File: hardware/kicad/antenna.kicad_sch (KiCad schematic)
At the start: 35 parts, among them J5 BWIPX-1-001E, J7 BWIPX-1-001E

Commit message: fix drc, layout and schematics
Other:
- note added: "Coplanar Waveguide With Ground Characteristic"
- note added: "Effective Dielectric Constant: 3.295 Characteristic Impedance: 49.9ohm"
- note added: "Relative Dielectric Constant: 4.56 Track Width : 0.33mm Gap Width : 0.2mm Dielectric Thickness : 0.1855mm"
- note added: "Trace Characteristic"
- note added: "Trace characteristics"
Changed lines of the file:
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@@
 	(title_block
 		(title "Antenna")
-		(date "2024-05-17")
-		(rev "1")
+		(date "2024-05-22")
+		(rev "2")
 		(company "Teapot Laboratories")
 	)
@@
 	(wire
 		(pts
-			(xy 85.09 121.793) (xy 81.28 121.793)
+			(xy 109.22 160.02) (xy 105.41 160.02)
 		)
 		(stroke
@@
 	(wire
 		(pts
-			(xy 85.09 117.983) (xy 85.09 121.793)
+			(xy 109.22 156.21) (xy 109.22 160.02)
 		)
 		(stroke
@@
 	)
 	(rectangle
+		(start 37.084 110.236)
+		(end 90.17 146.05)
+		(stroke
+			(width 0.5)
+			(type default)
+		)
+		(fill
+			(type none)
+		)
+	)
+	(rectangle
 		(start 93.345 38.735)
 		(end 279.4 146.05)
@@
 	)
 	(rectangle
-		(start 68.58 109.22)
-		(end 90.17 128.27)
+		(start 93.218 148.463)
+		(end 114.808 167.513)
 		(stroke
 			(width 0)
@@
 	(text "Sheets Connection"
 		(exclude_from_sim no)
-		(at 71.12 126.873 0)
+		(at 95.25 165.1 0)
 		(effects
 			(font
@@
 		)
 	)
+	(text "Trace characteristics"
+		(exclude_from_sim no)
+		(at 40.132 121.666 0)
+		(effects
+			(font
+				(size 1.27 1.27)
+				(thickness 0.254)
+				(bold yes)
+			)
+			(justify left bottom)
+		)
+	)
 	(text "EXT/TEST"
 		(exclude_from_sim no)
@@
 		)
 	)
+	(text "Coplanar Waveguide With Ground Characteristic"
+		(exclude_from_sim no)
+		(at 40.132 136.906 0)
+		(effects
+			(font
+				(size 1.27 1.27)
+				(thickness 0.254)
+				(bold yes)
+			)
+			(justify left bottom)
+		)
+	)
 	(text "GNSS Antenna Out"
 		(exclude_from_sim no)
@@
 		)
 	)
+	(text "Trace Characteristic"
+		(exclude_from_sim no)
+		(at 50.546 115.57 0)
+		(effects
+			(font
+				(size 2 2)
+				(thickness 0.4)
+				(bold yes)
+			)
+			(justify left bottom)
+		)
+	)
 	(text "place as close to the antenna feed"
 		(exclude_from_sim no)
@@
 		)
 	)
+	(text "Relative Dielectric Constant: 4.56\nTrack Width : 0.33mm\nGap Width : 0.2mm\nDielectric Thickness : 0.1855mm"
+		(exclude_from_sim no)
+		(at 40.132 131.064 0)
+		(effects
+			(font
+				(size 1.27 1.27)
+			)
+			(justify left bottom)
+		)
+	)
+	(text "Effective Dielectric Constant: 3.295\nCharacteristic Impedance: 49.9ohm"
+		(exclude_from_sim no)
+		(at 40.132 141.986 0)
+		(effects
+			(font
+				(size 1.27 1.27)
+			)
+			(justify left bottom)
+		)
+	)
 	(text "Matching Network\n"
 		(exclude_from_sim no)
@@
 	(hierarchical_label "+3V3"
 		(shape input)
-		(at 81.28 121.793 180)
+		(at 105.41 160.02 180)
 		(fields_autoplaced yes)
 		(effects
@@
 	(symbol
 		(lib_id "power:+3V3")
-		(at 85.09 117.983 0)
+		(at 109.22 156.21 0)
 		(mirror y)
 		(unit 1)
@@
 		(dnp no)
 		(property "Reference" "#PWR0114"
-			(at 85.09 121.793 0)
+			(at 109.22 160.02 0)
 			(effects
 				(font
@@
 		)
 		(property "Value" "+3V3"
-			(at 82.55 114.173 0)
+			(at 106.68 152.4 0)
 			(effects
 				(font
@@
 		)
 		(property "Footprint" ""
-			(at 85.09 117.983 0)
+			(at 109.22 156.21 0)
 			(effects
 				(font
@@
 		)
 		(property "Datasheet" ""
-			(at 85.09 117.983 0)
+			(at 109.22 156.21 0)
 			(effects
 				(font
@@
 		)
 		(property "Description" ""
-			(at 85.09 117.983 0)
+			(at 109.22 156.21 0)
 			(effects
 				(font

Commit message: finalizing board info
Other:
- note removed: "Coplanar Waveguide With Ground Characteristic"
- note removed: "Effective Dielectric Constant: 3.295 Characteristic Impedance: 49.9ohm"
- note removed: "Relative Dielectric Constant: 4.56 Track Width : 0.33mm Gap Width : 0.2mm Dielectric Thickness : 0.1855mm"
- note removed: "Trace Characteristic"
- note removed: "Trace characteristics"
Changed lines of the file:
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@@
 	(wire
 		(pts
-			(xy 109.22 160.02) (xy 105.41 160.02)
+			(xy 85.09 121.793) (xy 81.28 121.793)
 		)
 		(stroke
@@
 	(wire
 		(pts
-			(xy 109.22 156.21) (xy 109.22 160.02)
+			(xy 85.09 117.983) (xy 85.09 121.793)
 		)
 		(stroke
@@
 	)
 	(rectangle
-		(start 37.084 110.236)
-		(end 90.17 146.05)
-		(stroke
-			(width 0.5)
-			(type default)
-		)
-		(fill
-			(type none)
-		)
-	)
-	(rectangle
 		(start 93.345 38.735)
 		(end 279.4 146.05)
@@
 	)
 	(rectangle
-		(start 93.218 148.463)
-		(end 114.808 167.513)
+		(start 68.58 109.22)
+		(end 90.17 128.27)
 		(stroke
 			(width 0)
@@
 	(text "Sheets Connection"
 		(exclude_from_sim no)
-		(at 95.25 165.1 0)
+		(at 71.12 126.873 0)
 		(effects
 			(font
@@
 		)
 	)
-	(text "Trace characteristics"
-		(exclude_from_sim no)
-		(at 40.132 121.666 0)
-		(effects
-			(font
-				(size 1.27 1.27)
-				(thickness 0.254)
-				(bold yes)
-			)
-			(justify left bottom)
-		)
-	)
 	(text "EXT/TEST"
 		(exclude_from_sim no)
@@
 		)
 	)
-	(text "Coplanar Waveguide With Ground Characteristic"
-		(exclude_from_sim no)
-		(at 40.132 136.906 0)
-		(effects
-			(font
-				(size 1.27 1.27)
-				(thickness 0.254)
-				(bold yes)
-			)
-			(justify left bottom)
-		)
-	)
 	(text "GNSS Antenna Out"
 		(exclude_from_sim no)
@@
 		)
 	)
-	(text "Trace Characteristic"
-		(exclude_from_sim no)
-		(at 50.546 115.57 0)
-		(effects
-			(font
-				(size 2 2)
-				(thickness 0.4)
-				(bold yes)
-			)
-			(justify left bottom)
-		)
-	)
 	(text "place as close to the antenna feed"
 		(exclude_from_sim no)
@@
 		)
 	)
-	(text "Relative Dielectric Constant: 4.56\nTrack Width : 0.33mm\nGap Width : 0.2mm\nDielectric Thickness : 0.1855mm"
-		(exclude_from_sim no)
-		(at 40.132 131.064 0)
-		(effects
-			(font
-				(size 1.27 1.27)
-			)
-			(justify left bottom)
-		)
-	)
-	(text "Effective Dielectric Constant: 3.295\nCharacteristic Impedance: 49.9ohm"
-		(exclude_from_sim no)
-		(at 40.132 141.986 0)
-		(effects
-			(font
-				(size 1.27 1.27)
-			)
-			(justify left bottom)
-		)
-	)
 	(text "Matching Network\n"
 		(exclude_from_sim no)
@@
 	(hierarchical_label "+3V3"
 		(shape input)
-		(at 105.41 160.02 180)
+		(at 81.28 121.793 180)
 		(fields_autoplaced yes)
 		(effects
@@
 	(symbol
 		(lib_id "power:+3V3")
-		(at 109.22 156.21 0)
+		(at 85.09 117.983 0)
 		(mirror y)
 		(unit 1)
@@
 		(dnp no)
 		(property "Reference" "#PWR0114"
-			(at 109.22 160.02 0)
+			(at 85.09 121.793 0)
 			(effects
 				(font
@@
 		)
 		(property "Value" "+3V3"
-			(at 106.68 152.4 0)
+			(at 82.55 114.173 0)
 			(effects
 				(font
@@
 		)
 		(property "Footprint" ""
-			(at 109.22 156.21 0)
+			(at 85.09 117.983 0)
 			(effects
 				(font
@@
 		)
 		(property "Datasheet" ""
-			(at 109.22 156.21 0)
+			(at 85.09 117.983 0)
 			(effects
 				(font
@@
 		)
 		(property "Description" ""
-			(at 109.22 156.21 0)
+			(at 85.09 117.983 0)
 			(effects
 				(font

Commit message: Start Rev 3
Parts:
- removed C48, C49: DNP, Capacitor_SMD:C_0402_1005Metric, symbol Device:C_Small
- removed D3: ESD5651N, Diode_SMD:D_SOD-882, symbol Device:D_TVS
- removed E1: NN03-320, bwlc1a:NN03-320, symbol bwlc1a:NN03-320
- removed J5: BWIPX-1-001E, bwlc1a:BWIPX-1-001E, symbol bwlc1a:BWIPX-1-001E
- removed L1: 10n, Inductor_SMD:L_0603_1608Metric, symbol Device:L
- removed L2: 9n5, Inductor_SMD:L_0603_1608Metric, symbol Device:L
- removed R24, R35, R36, R37: 0, Resistor_SMD:R_0402_1005Metric, symbol Device:R_Small
- removed R38: 0, Resistor_SMD:R_0603_1608Metric, symbol Device:R_Small
- removed R40: DNP, Resistor_SMD:R_0402_1005Metric, symbol Device:R_Small
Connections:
- no-connect marks 3 -> 0

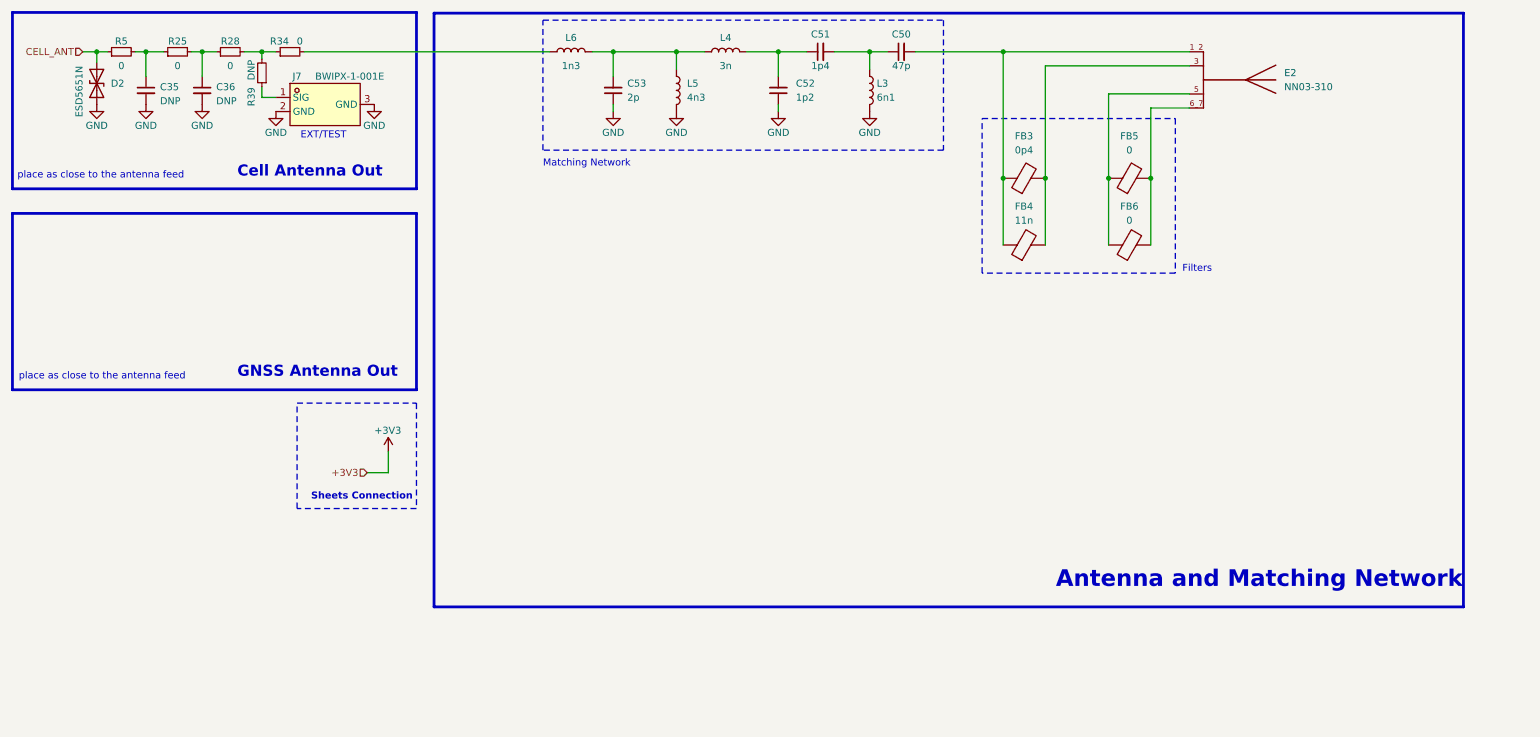
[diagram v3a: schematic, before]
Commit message: GNSS and Antenna Update
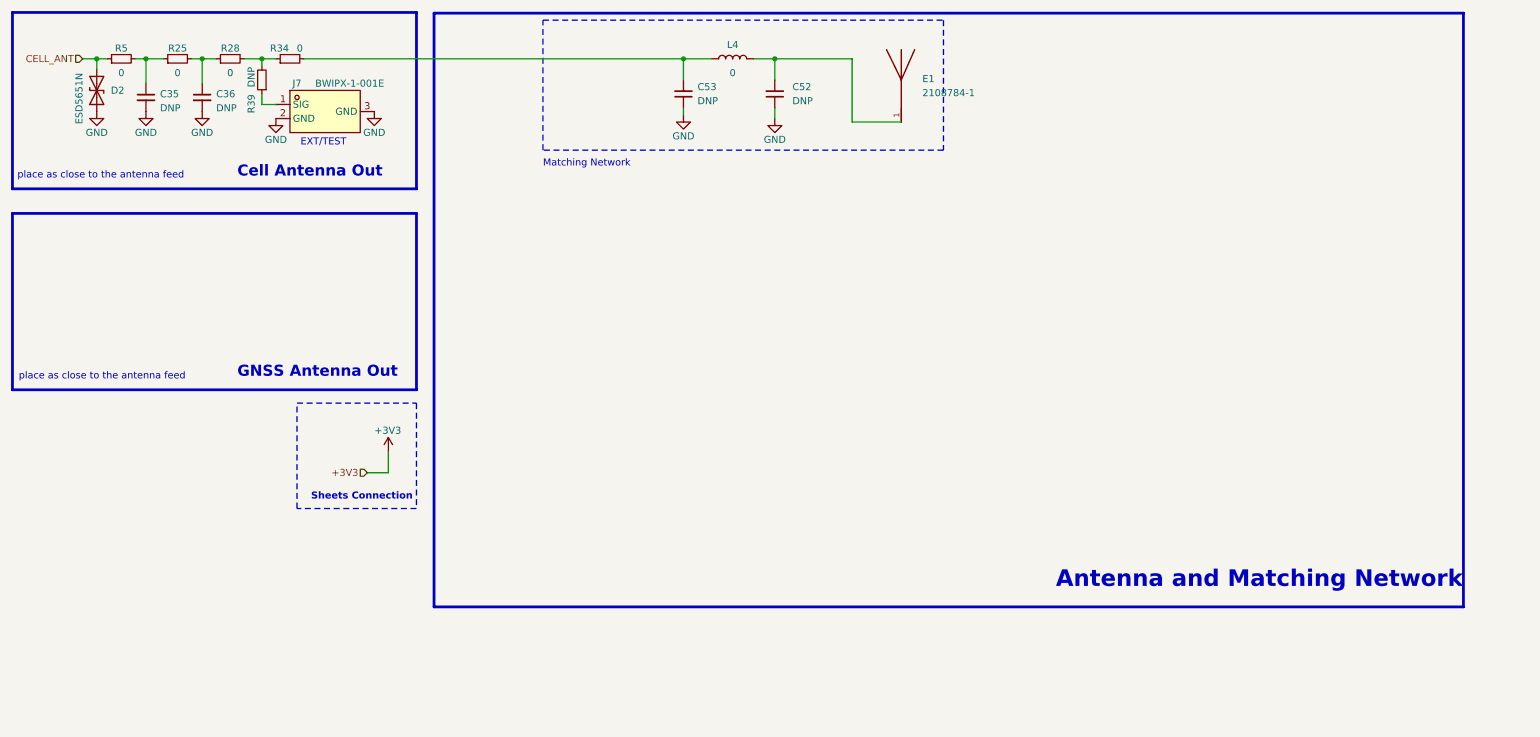
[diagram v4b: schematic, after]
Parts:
- removed C50: 47p, Capacitor_SMD:C_0402_1005Metric, symbol Device:C_Small
- removed C51: 1p4, Capacitor_SMD:C_0402_1005Metric, symbol Device:C_Small
- removed E2: NN03-310, bwlc1a:NN03-310, symbol bwlc1a:NN03-310
- removed FB3: 0p4, Inductor_SMD:L_0402_1005Metric, symbol Device:FerriteBead
- removed FB4: 11n, Inductor_SMD:L_0603_1608Metric, symbol Device:FerriteBead
- removed FB5: 0, Inductor_SMD:L_0402_1005Metric, symbol Device:FerriteBead
- removed FB6: 0, Inductor_SMD:L_0603_1608Metric, symbol Device:FerriteBead
- removed L3: 6n1, Inductor_SMD:L_0402_1005Metric, symbol Device:L
- removed L5: 4n3, Inductor_SMD:L_0603_1608Metric, symbol Device:L
- removed L6: 1n3, Inductor_SMD:L_0402_1005Metric, symbol Device:L
- added E1: 2108784-1, bwlc1a:2108784-1, symbol bwlc1a:2108784-1
- C52: value 1p2 -> DNP
- C53: value 2p -> DNP
- L4: value 3n -> 0
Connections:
- net at R34.2: now also C53.2, L4.1
- net at C52.2, L4.2: now also E1.1
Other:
- note removed: "Filters"
- moved on the sheet: C35, C36, C52, C53, D2, J7, L4, R25, R28, R34, R39, R5

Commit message: Update for PCB Layout
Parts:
- renumbered C53 to C39, C52 to C40, C35 to C41, C36 to C42, D2 to D12, J7 to J6, L4 to L2, R5 to R33, R25 to R34, R28 to R35, R34 to R36, R39 to R37
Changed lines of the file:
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@@
 		(dnp no)
 		(fields_autoplaced yes)
-		(property "Reference" "C36"
+		(property "Reference" "C42"
 			(at 53.975 53.3463 0)
 			(effects
@@
 			(project "bwlc1a"
 				(path "/388039b1-99cc-430f-bd4a-010573fde798/ca79f09e-abdb-462a-9aab-98f2e37e5b23"
-					(reference "C36")
+					(reference "C42")
 					(unit 1)
 				)
@@
 		(on_board yes)
 		(dnp no)
-		(property "Reference" "R34"
+		(property "Reference" "R36"
 			(at 65.405 45.085 90)
 			(effects
@@
 			(project "bwlc1a"
 				(path "/388039b1-99cc-430f-bd4a-010573fde798/ca79f09e-abdb-462a-9aab-98f2e37e5b23"
-					(reference "R34")
+					(reference "R36")
 					(unit 1)
 				)
@@
 		(on_board yes)
 		(dnp no)
-		(property "Reference" "#PWR072"
+		(property "Reference" "#PWR0110"
 			(at 51.435 62.865 0)
 			(effects
@@
 			(project "bwlc1a"
 				(path "/388039b1-99cc-430f-bd4a-010573fde798/ca79f09e-abdb-462a-9aab-98f2e37e5b23"
-					(reference "#PWR072")
+					(reference "#PWR0110")
 					(unit 1)
 				)
@@
 		(on_board yes)
 		(dnp no)
-		(property "Reference" "#PWR0112"
+		(property "Reference" "#PWR0114"
 			(at 154.94 64.135 0)
 			(effects
@@
 			(project "bwlc1a"
 				(path "/388039b1-99cc-430f-bd4a-010573fde798/ca79f09e-abdb-462a-9aab-98f2e37e5b23"
-					(reference "#PWR0112")
+					(reference "#PWR0114")
 					(unit 1)
 				)
@@
 		(on_board yes)
 		(dnp no)
-		(property "Reference" "R39"
+		(property "Reference" "R37"
 			(at 60.325 55.118 90)
 			(effects
@@
 			(project "bwlc1a"
 				(path "/388039b1-99cc-430f-bd4a-010573fde798/ca79f09e-abdb-462a-9aab-98f2e37e5b23"
-					(reference "R39")
+					(reference "R37")
 					(unit 1)
 				)
@@
 		(on_board yes)
 		(dnp no)
-		(property "Reference" "D2"
+		(property "Reference" "D12"
 			(at 34.925 52.705 90)
 			(effects
@@
 			(project "bwlc1a"
 				(path "/388039b1-99cc-430f-bd4a-010573fde798/ca79f09e-abdb-462a-9aab-98f2e37e5b23"
-					(reference "D2")
+					(reference "D12")
 					(unit 1)
 				)
@@
 		(dnp no)
 		(fields_autoplaced yes)
-		(property "Reference" "C53"
+		(property "Reference" "C39"
 			(at 140.97 52.0635 0)
 			(effects
@@
 			(project "bwlc1a"
 				(path "/388039b1-99cc-430f-bd4a-010573fde798/ca79f09e-abdb-462a-9aab-98f2e37e5b23"
-					(reference "C53")
+					(reference "C39")
 					(unit 1)
 				)
@@
 		(on_board yes)
 		(dnp no)
-		(property "Reference" "#PWR026"
+		(property "Reference" "#PWR0109"
 			(at 41.275 62.865 0)
 			(effects
@@
 			(project "bwlc1a"
 				(path "/388039b1-99cc-430f-bd4a-010573fde798/ca79f09e-abdb-462a-9aab-98f2e37e5b23"
-					(reference "#PWR026")
+					(reference "#PWR0109")
 					(unit 1)
 				)
@@
 		(on_board yes)
 		(dnp no)
-		(property "Reference" "R5"
+		(property "Reference" "R33"
 			(at 36.83 45.085 90)
 			(effects
@@
 			(project "bwlc1a"
 				(path "/388039b1-99cc-430f-bd4a-010573fde798/ca79f09e-abdb-462a-9aab-98f2e37e5b23"
-					(reference "R5")
+					(reference "R33")
 					(unit 1)
 				)
@@
 		(on_board yes)
 		(dnp no)
-		(property "Reference" "#PWR0121"
+		(property "Reference" "#PWR0108"
 			(at 32.385 62.865 0)
 			(effects
@@
 			(project "bwlc1a"
 				(path "/388039b1-99cc-430f-bd4a-010573fde798/ca79f09e-abdb-462a-9aab-98f2e37e5b23"
-					(reference "#PWR0121")
+					(reference "#PWR0108")
 					(unit 1)
 				)
@@
 		(on_board yes)
 		(dnp no)
-		(property "Reference" "L4"
+		(property "Reference" "L2"
 			(at 147.32 44.45 90)
 			(effects
@@
 			(project "bwlc1a"
 				(path "/388039b1-99cc-430f-bd4a-010573fde798/ca79f09e-abdb-462a-9aab-98f2e37e5b23"
-					(reference "L4")
+					(reference "L2")
 					(unit 1)
 				)
@@
 		(dnp no)
 		(fields_autoplaced yes)
-		(property "Reference" "C35"
+		(property "Reference" "C41"
 			(at 43.815 53.3463 0)
 			(effects
@@
 			(project "bwlc1a"
 				(path "/388039b1-99cc-430f-bd4a-010573fde798/ca79f09e-abdb-462a-9aab-98f2e37e5b23"
-					(reference "C35")
+					(reference "C41")
 					(unit 1)
 				)
@@
 		(on_board yes)
 		(dnp no)
-		(property "Reference" "R28"
+		(property "Reference" "R35"
 			(at 56.515 45.085 90)
 			(effects
@@
 			(project "bwlc1a"
 				(path "/388039b1-99cc-430f-bd4a-010573fde798/ca79f09e-abdb-462a-9aab-98f2e37e5b23"
-					(reference "R28")
+					(reference "R35")
 					(unit 1)
 				)
@@
 		(on_board yes)
 		(dnp no)
-		(property "Reference" "#PWR020"
+		(property "Reference" "#PWR0112"
 			(at 138.43 63.5 0)
 			(effects
@@
 			(project "bwlc1a"
 				(path "/388039b1-99cc-430f-bd4a-010573fde798/ca79f09e-abdb-462a-9aab-98f2e37e5b23"
-					(reference "#PWR020")
+					(reference "#PWR0112")
 					(unit 1)
 				)
@@
 		(on_board yes)
 		(dnp no)
-		(property "Reference" "#PWR0114"
+		(property "Reference" "#PWR0115"
 			(at 85.09 121.793 0)
 			(effects
@@
 			(project "bwlc1a"
 				(path "/388039b1-99cc-430f-bd4a-010573fde798/ca79f09e-abdb-462a-9aab-98f2e37e5b23"
-					(reference "#PWR0114")
+					(reference "#PWR0115")
 					(unit 1)
 				)
@@
 		(on_board yes)
 		(dnp no)
-		(property "Reference" "#PWR0128"
+		(property "Reference" "#PWR0111"
 			(at 82.55 62.865 0)
 			(effects
@@
 			(project "bwlc1a"
 				(path "/388039b1-99cc-430f-bd4a-010573fde798/ca79f09e-abdb-462a-9aab-98f2e37e5b23"
-					(reference "#PWR0128")
+					(reference "#PWR0111")
 					(unit 1)
 				)
@@
 		(on_board yes)
 		(dnp no)
-		(property "Reference" "J7"
+		(property "Reference" "J6"
 			(at 68.58 51.435 0)
 			(effects
@@
 			(project "bwlc1a"
 				(path "/388039b1-99cc-430f-bd4a-010573fde798/ca79f09e-abdb-462a-9aab-98f2e37e5b23"
-					(reference "J7")
+					(reference "J6")
 					(unit 1)
 				)
@@
 		(on_board yes)
 		(dnp no)
-		(property "Reference" "R25"
+		(property "Reference" "R34"
 			(at 46.99 45.085 90)
 			(effects
@@
 			(project "bwlc1a"
 				(path "/388039b1-99cc-430f-bd4a-010573fde798/ca79f09e-abdb-462a-9aab-98f2e37e5b23"
-					(reference "R25")
+					(reference "R34")
 					(unit 1)
 				)
@@
 		(dnp no)
 		(fields_autoplaced yes)
-		(property "Reference" "C52"
+		(property "Reference" "C40"
 			(at 158.115 52.0635 0)
 			(effects
@@
 			(project "bwlc1a"
 				(path "/388039b1-99cc-430f-bd4a-010573fde798/ca79f09e-abdb-462a-9aab-98f2e37e5b23"
-					(reference "C52")
+					(reference "C40")
 					(unit 1)
 				)
@@
 		(on_board yes)
 		(dnp no)
-		(property "Reference" "#PWR0127"
+		(property "Reference" "#PWR0113"
 			(at 64.77 64.135 0)
 			(effects
@@
 			(project "bwlc1a"
 				(path "/388039b1-99cc-430f-bd4a-010573fde798/ca79f09e-abdb-462a-9aab-98f2e37e5b23"
-					(reference "#PWR0127")
-					(unit 1)
-				)
+					(reference "#PWR0113")
+					(unit 1)
+				)

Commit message: Finish Manufacturing File
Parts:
- C39: Distributor LCSC -> -; Distributor Link https://www.lcsc.com/product-detail/Multilayer-Ceramic-Capa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 -> -; Distributor Part Number C88885 -> -; Manufacturer Murata Electronics -> -; Manufacturer Part Number GJM1555C1H2R0WB01D -> -
- C40: Distributor LCSC -> -; Distributor Link https://www.lcsc.com/product-detail/Multilayer-Ceramic-Capa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 -> -; Distributor Part Number C76899 -> -; Manufacturer Murata Electronics -> -; Manufacturer Part Number GJM1555C1H1R2WB01D -> -
- C41, C42: Distributor (none) -> -; Distributor Link (none) -> -; Distributor Part Number (none) -> -; Manufacturer (none) -> -; Manufacturer Part Number (none) -> -
- E1: Distributor (none) -> TE Connectivity; Distributor Link (none) -> https://www.te.com/en/product-2108784-1.html; Distributor Part Number (none) -> -; Manufacturer (none) -> TE Connectivity; Manufacturer Part Number (none) -> 2108784-1
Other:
- note removed: "GNSS Antenna Out"
- note removed: "Matching Network"
- moved on the sheet: C39, C40, C41, C42, D12, E1, J6, L2, R33, R34, R35, R36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
